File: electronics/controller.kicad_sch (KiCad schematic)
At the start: 90 parts, among them J1 Power_Supply_Connector, J10 Heated_Bed_Thermistor_Connect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, J11 Bl_Touch_Gnd_ZMin_Connector, J12 Bl_Touch_Signal_Vcc_Gnd_Conne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, J13 Motor_A_Connector, J14 Motor_B_Connector, J15 Motor_Z_Connector, J16 Motor_E_Connector, J2 X_Axis_Endstop_Connector, J3 Y_Axis_Endstop_Connector, J4 USB_C_Receptacle_USB2.0, J5 Hotend_Connector, J6 Heated_Bed_Connector, J7 Hotend_Fan_Connector, J8 Layer_Fan_Connector, J9 Hotend_Thermistor_Connector, Q1 SIA440DJ-T1-GE3, Q2 SISS76LDN-T1-GE3, Q3 SIA440DJ-T1-GE3, Q4 SIA440DJ-T1-GE3, SW1 EN_Button, SW2 Boot_Button, SW3 Pause/Resume_Button, U1 AZ1084CD-3.3TRG1, U10 MCU45P04-TP, U11 K7805MT-1000R4, U3 ESP32-S3-WROOM-1, U4 MT29F2G01ABAGDWB-IT, U5 USBLC6-2SC6, U6 TMC2209_SILENTSTEPSTICK, U7 TMC2209_SILENTSTEPSTICK, U8 TMC2209_SILENTSTEPSTICK, U9 TMC2209_SILENTSTEPSTICK

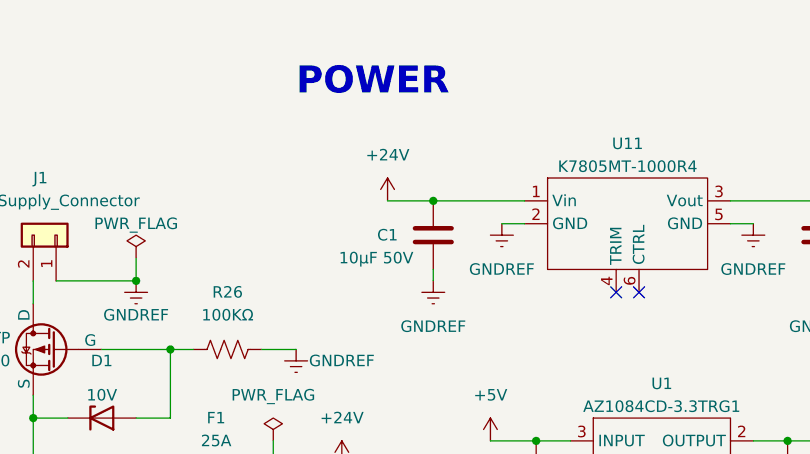
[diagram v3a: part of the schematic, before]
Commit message: ✨ Add overcurrent protection on 5V regulator
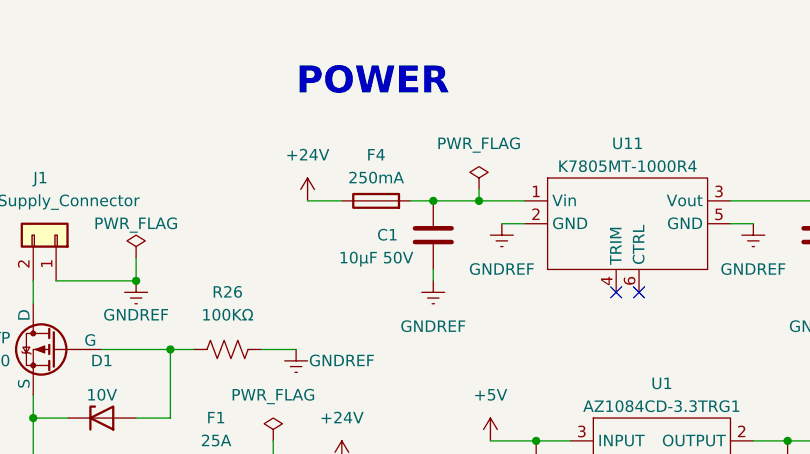
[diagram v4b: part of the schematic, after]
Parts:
- added F4: 250mA, symbol Project:Fuse
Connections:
- net +24V: now also F4.1; no longer C1.2, U11.1 (Vin)
- new net: C1.2, F4.2, U11.1 (Vin)
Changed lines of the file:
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@@
   (junction (at 212.09 194.31) (diameter 0) (color 0 0 0 0)
   )
+  (junction (at 76.2 31.75) (diameter 0) (color 0 0 0 0)
+  )
   (junction (at 311.15 175.26) (diameter 0) (color 0 0 0 0)
   )
@@
   (junction (at 374.65 179.07) (diameter 0) (color 0 0 0 0)
   )
-  (junction (at 76.2 31.75) (diameter 0) (color 0 0 0 0)
-  )
   (junction (at 119.38 31.75) (diameter 0) (color 0 0 0 0)
   )
@@
   (junction (at 58.42 104.14) (diameter 0) (color 0 0 0 0)
   )
+  (junction (at 81.28 31.75) (diameter 0) (color 0 0 0 0)
+  )
   (junction (at 320.04 116.84) (diameter 0) (color 0 0 0 0)
   )
@@
     (stroke (width 0) (type default))
   )
+  (wire (pts (xy 81.28 31.75) (xy 86.36 31.75))
+    (stroke (width 0) (type default))
+  )
   (wire (pts (xy 161.29 43.18) (xy 166.37 43.18))
     (stroke (width 0) (type default))
@@
     (stroke (width 0) (type default))
   )
+  (wire (pts (xy 76.2 31.75) (xy 81.28 31.75))
+    (stroke (width 0) (type default))
+  )
   (wire (pts (xy 256.54 93.98) (xy 283.21 93.98))
     (stroke (width 0) (type default))
@@
     (stroke (width 0) (type default))
   )
+  (wire (pts (xy 73.66 31.75) (xy 76.2 31.75))
+    (stroke (width 0) (type default))
+  )
   (wire (pts (xy 115.57 66.04) (xy 115.57 67.31))
     (stroke (width 0) (type default))
@@
     (stroke (width 0) (type default))
   )
-  (wire (pts (xy 76.2 31.75) (xy 86.36 31.75))
-    (stroke (width 0) (type default))
-  )
   (wire (pts (xy 298.45 193.04) (xy 302.26 193.04))
     (stroke (width 0) (type default))
@@
     (stroke (width 0) (type default))
   )
+  (wire (pts (xy 62.23 31.75) (xy 66.04 31.75))
+    (stroke (width 0) (type default))
+  )
   (wire (pts (xy 85.09 231.14) (xy 85.09 234.95))
     (stroke (width 0) (type default))
@@
     (stroke (width 0) (type default))
   )
-  (wire (pts (xy 71.12 31.75) (xy 76.2 31.75))
-    (stroke (width 0) (type default))
-  )
   (wire (pts (xy 326.39 34.29) (xy 331.47 34.29))
     (stroke (width 0) (type default))
@@
     (stroke (width 0) (type default))
   )
+  (wire (pts (xy 81.28 30.48) (xy 81.28 31.75))
+    (stroke (width 0) (type default))
+  )
   (wire (pts (xy 113.03 198.12) (xy 124.46 198.12))
     (stroke (width 0) (type default))
@@
     )
   )
-  (symbol (lib_id "Project:+24V") (at 71.12 31.75 0) (unit 1)
+  (symbol (lib_id "Project:+24V") (at 62.23 31.75 0) (unit 1)
     (in_bom yes) (on_board yes) (dnp no) (fields_autoplaced)
-    (property "Reference" "#PWR093" (at 71.12 35.56 0)
+    (property "Reference" "#PWR093" (at 62.23 35.56 0)
       (effects (font (size 1.27 1.27)) hide)
     )
-    (property "Value" "+24V" (at 71.12 26.67 0)
+    (property "Value" "+24V" (at 62.23 26.67 0)
       (effects (font (size 1.27 1.27)))
     )
-    (property "Footprint" "" (at 71.12 31.75 0)
+    (property "Footprint" "" (at 62.23 31.75 0)
       (effects (font (size 1.27 1.27)) hide)
     )
-    (property "Datasheet" "" (at 71.12 31.75 0)
+    (property "Datasheet" "" (at 62.23 31.75 0)
       (effects (font (size 1.27 1.27)) hide)
     )
@@
     )
   )
+  (symbol (lib_id "Project:PWR_FLAG") (at 81.28 30.48 0) (unit 1)
+    (in_bom yes) (on_board yes) (dnp no) (fields_autoplaced)
+    (property "Reference" "#FLG02" (at 81.28 28.575 0)
+      (effects (font (size 1.27 1.27)) hide)
+    )
+    (property "Value" "PWR_FLAG" (at 81.28 25.4 0)
+      (effects (font (size 1.27 1.27)))
+    )
+    (property "Footprint" "" (at 81.28 30.48 0)
+      (effects (font (size 1.27 1.27)) hide)
+    )
+    (property "Datasheet" "~" (at 81.28 30.48 0)
+      (effects (font (size 1.27 1.27)) hide)
+    )
+    (pin "1")
+    (instances
+      (project "controller"
+        (path "/b72cfb6e-763f-4aec-88af-02f682ab9e2d"
+          (reference "#FLG02") (unit 1)
+        )
+      )
+    )
+  )
   (symbol (lib_id "Project:GNDREF") (at 160.02 213.36 0) (unit 1)
     (in_bom yes) (on_board yes) (dnp no) (fields_autoplaced)
@@
         )
       )
+    )
+  )
+  (symbol (lib_id "Project:Fuse") (at 69.85 31.75 90) (unit 1)
+    (in_bom yes) (on_board yes) (dnp no) (fields_autoplaced)
+    (property "Reference" "F4" (at 69.85 26.67 90)
+      (effects (font (size 1.27 1.27)))
+    )
+    (property "Value" "250mA" (at 69.85 29.21 90)
+      (effects (font (size 1.27 1.27)))
+    )
+    (property "Footprint" "" (at 69.85 33.528 90)
+      (effects (font (size 1.27 1.27)) hide)
+    )
+    (property "Datasheet" "~" (at 69.85 31.75 0)
+      (effects (font (size 1.27 1.27)) hide)
+    )
+    (pin "1")
+    (pin "2")
+    (instances
+      (project "controller"
+        (path "/b72cfb6e-763f-4aec-88af-02f682ab9e2d"
+          (reference "F4") (unit 1)
+        )
+      )

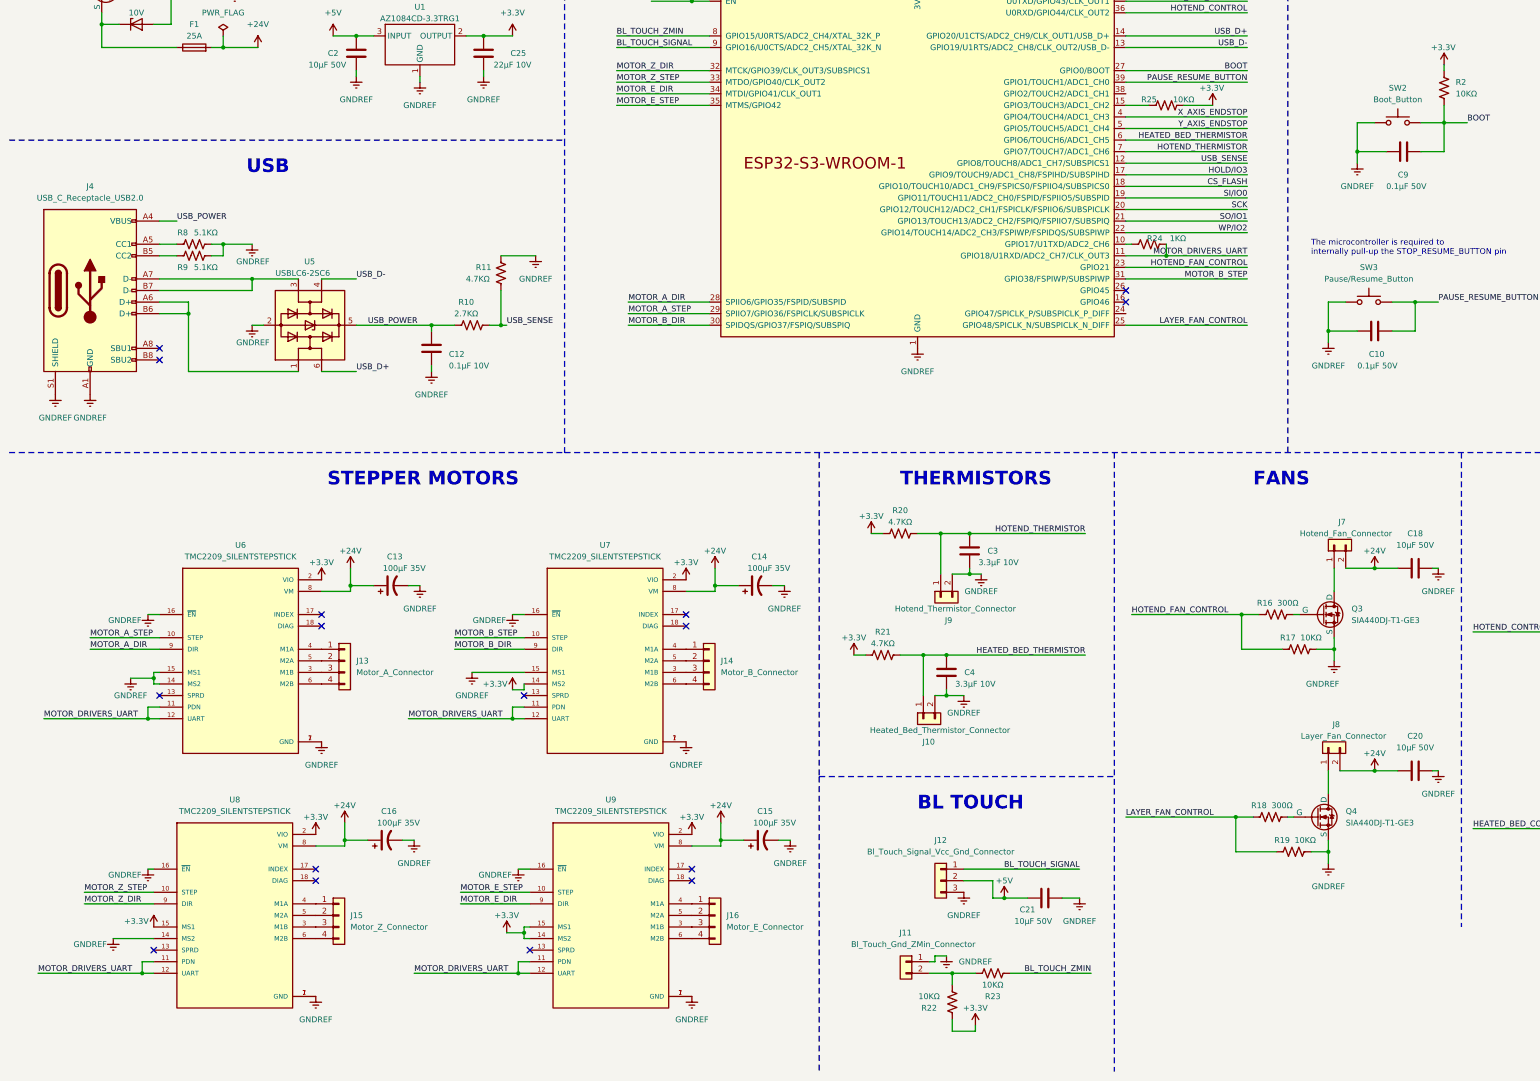
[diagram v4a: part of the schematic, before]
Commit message: ✨ Add extra connectors for unused pins on KiCad schematic
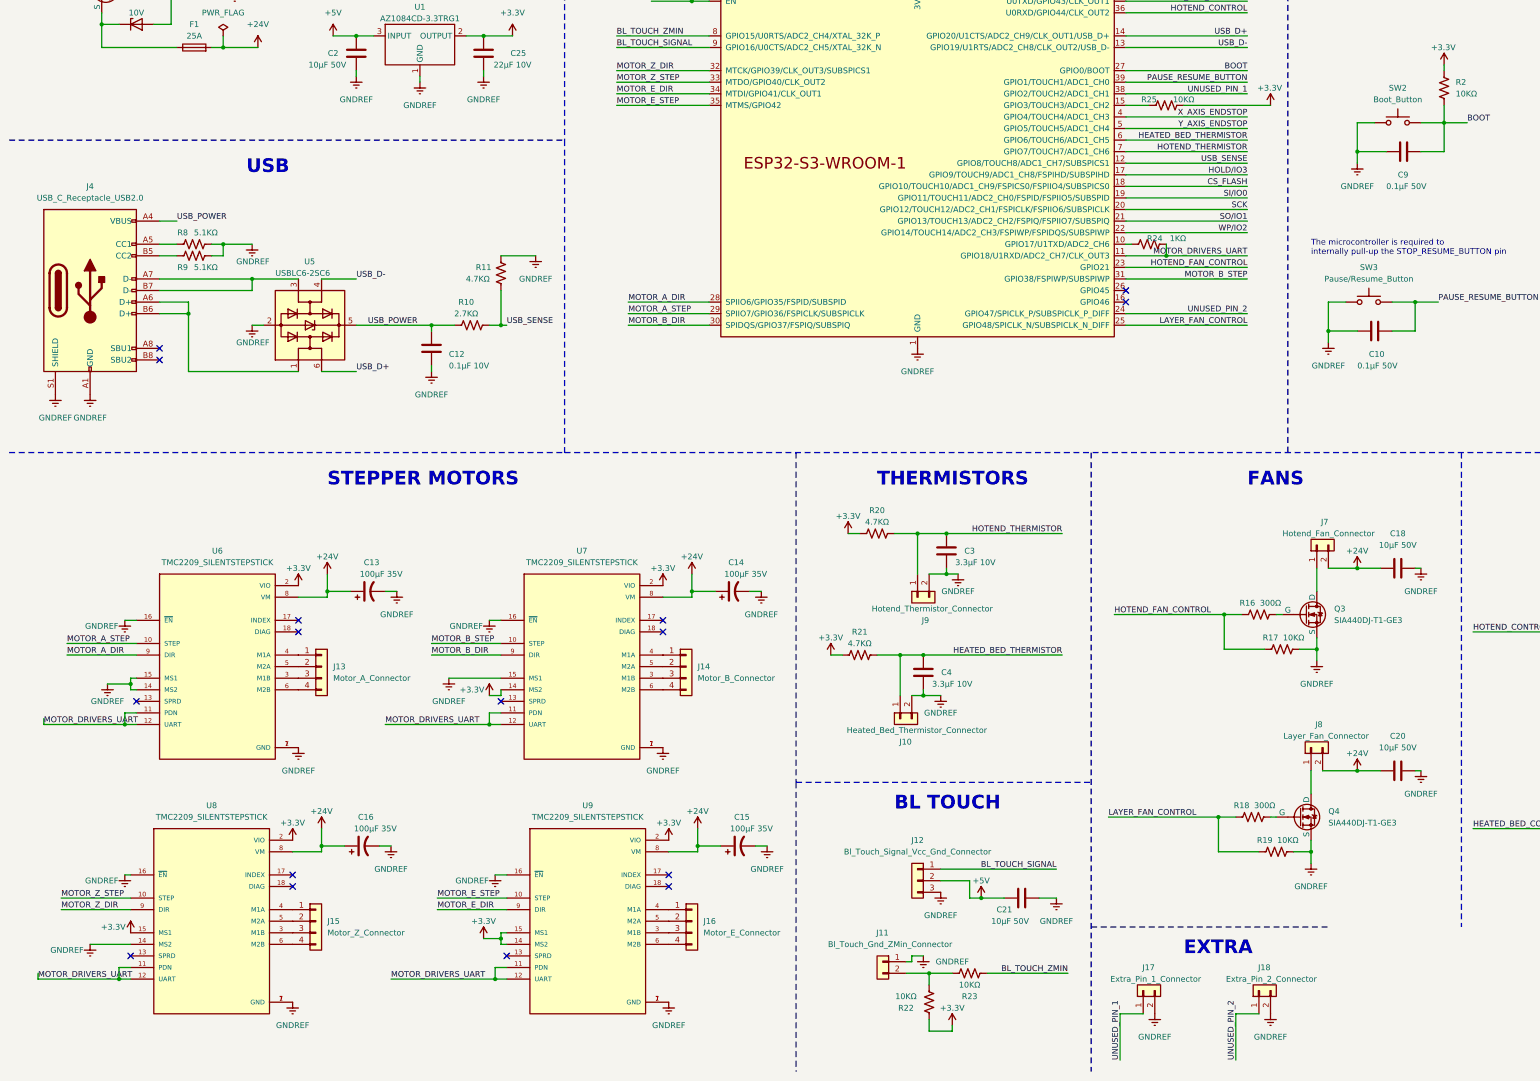
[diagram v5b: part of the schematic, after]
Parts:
- added J17: Extra_Pin_1_Connector, symbol Project:Conn_01x02
- added J18: Extra_Pin_2_Connector, symbol Project:Conn_01x02
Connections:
- net GNDREF: now also J17.2 (Pin_2), J18.2 (Pin_2)
- net UNUSED_PIN_2: now reaches U3.24 (GPIO47/SPICLK_P/SUBSPICLK_P_DIFF)
- net UNUSED_PIN_2: now also J18.1 (Pin_1)
- net UNUSED_PIN_1: now reaches U3.38 (GPIO2/TOUCH2/ADC1_CH1)
- net UNUSED_PIN_1: now also J17.1 (Pin_1)
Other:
- note added: "EXTRA"
- moved on the sheet: C13, C14, C15, C16, C18, C20, C21, C3, C4, J10, J11, J12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

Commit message: 🔖 Revision 1.0 of KiCad schematic
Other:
- title: (none) -> ESP32-S3 3D printer controller
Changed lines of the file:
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@@
 (kicad_sch (version 20230121) (generator eeschema)
   (paper "A3")
+  (title_block
+    (title "ESP32-S3 3D printer controller")
+    (date "2023-10-15")
+    (rev "1.0")
+  )
   (junction (at 224.79 247.65) (diameter 0) (color 0 0 0 0)
   )

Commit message: 🚧 Assign footprints to some components
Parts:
- C1, C10, C11, C12, C17, C18, C19, C2, C20, C21, C22, C23, C24, C25, C3, C4, C5, C6, C7, C8, C9: footprint (none) -> Capacitor_SMD:C_1206_3216Metric_Pad1.33x1.80mm_HandSolder
- C13, C14, C15, C16: footprint (none) -> Capacitor_THT:CP_Radial_D6.3mm_P2.50mm
- D1: footprint (none) -> Diode_SMD:D_SOD-123
- D2: footprint (none) -> Project:SMADO-214AC_LEAD-FRAME_MCC-L
- D3: value SDT30B100D1-13 -> SK510A-LTP; footprint (none) -> Project:SMADO-214AC_LEAD-FRAME_MCC-L
- F1, F2, F3, F4: footprint (none) -> Fuse:Fuse_1206_3216Metric_Pad1.42x1.75mm_HandSolder
- J1: footprint (none) -> TerminalBlock_Phoenix:TerminalBlock_Phoenix_MKDS-1,5-2-5.08_1x02_P5.08mm_Horizontal
- J10, J11, J17, J18, J5, J7, J8, J9, SW3: footprint (none) -> Connector_Wire:SolderWire-0.5sqmm_1x02_P4.6mm_D0.9mm_OD2.1mm
- J12, J2, J3: footprint (none) -> Connector_Wire:SolderWire-0.5sqmm_1x03_P4.6mm_D0.9mm_OD2.1mm
- J13, J14, J15, J16: footprint (none) -> Connector_Wire:SolderWire-0.5sqmm_1x04_P4.6mm_D0.9mm_OD2.1mm
- J4: footprint (none) -> Connector_USB:USB_C_Receptacle_GCT_USB4105-xx-A_16P_TopMnt_Horizontal
- Q1, Q3, Q4: footprint Package_TO_SOT_SMD:LFPAK56 -> Project:Vishay_PowerPAK_SC70-6L_Single
- Q2: footprint Package_TO_SOT_SMD:LFPAK56 -> Project:PowerPAK® 1212-8SH
- R1, R10, R11, R12, R13, R14, R15, R16, R17, R18, R19, R2, R20, R21, R22, R23, R24, R25, R26, R3, R4, R5, R6, R7, R8, R9: footprint (none) -> Resistor_SMD:R_1206_3216Metric_Pad1.30x1.75mm_HandSolder
- SW1, SW2: footprint (none) -> Button_Switch_THT:SW_PUSH_6mm
- U1, U10: footprint (none) -> Package_TO_SOT_SMD:TO-252-3_TabPin2
- U4: footprint (none) -> Project:U-PDFN (MLP8)
- U6, U7, U8, U9: footprint MODULE_TMC2209_SILENTSTEPSTICK -> Project:MODULE_TMC2209_SILENTSTEPSTICK
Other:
- moved on the sheet: Q2, R14, R15

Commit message: ✨ Add footprints of remaining components on KiCad
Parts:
- J6: footprint (none) -> Project:SolderWire-2.5sqmm_1x02_P7.2mm_D2.4mm_OD3.6mm
- U11: footprint (none) -> Project:MODULE_6-SMD
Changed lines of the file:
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@@
       (effects (font (size 1.27 1.27)))
     )
-    (property "Footprint" "" (at 97.79 33.02 0)
+    (property "Footprint" "Project:MODULE_6-SMD" (at 97.79 33.02 0)
       (effects (font (size 1.27 1.27)) hide)
     )
@@
       (effects (font (size 1.27 1.27)) (justify left))
     )
-    (property "Footprint" "" (at 377.19 213.36 0)
+    (property "Footprint" "Project:SolderWire-2.5sqmm_1x02_P7.2mm_D2.4mm_OD3.6mm" (at 377.19 213.36 0)
       (effects (font (size 1.27 1.27)) hide)
     )
